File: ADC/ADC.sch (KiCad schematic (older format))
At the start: 89 parts

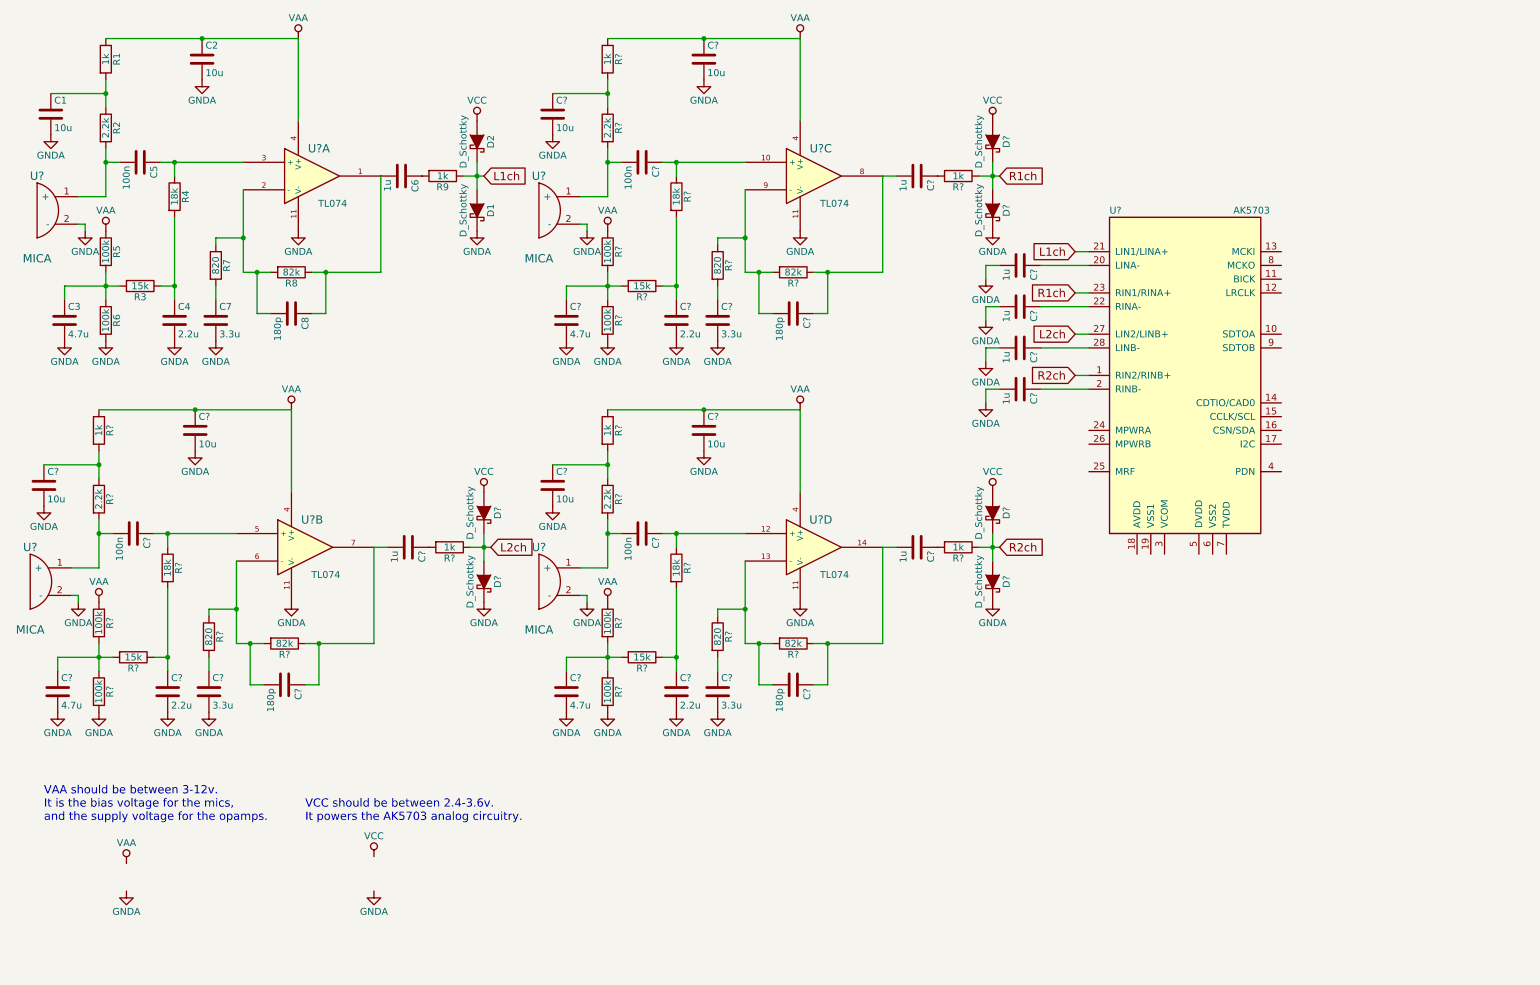
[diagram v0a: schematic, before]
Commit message: Finished Digital Section
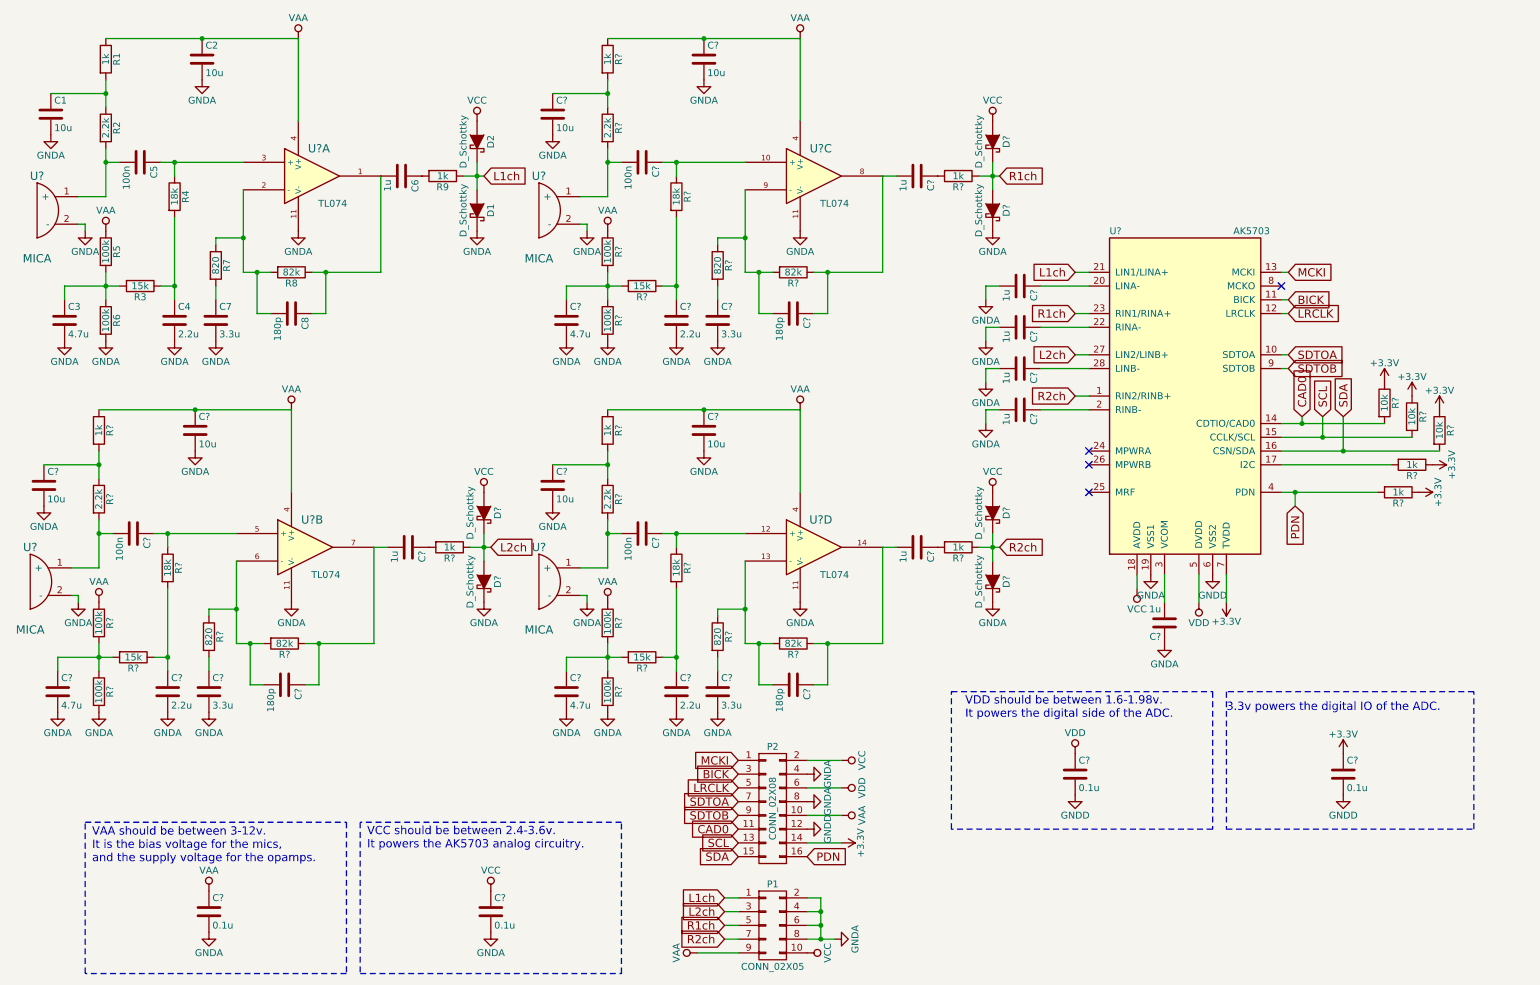
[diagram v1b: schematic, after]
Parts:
- added C?: 1u, symbol C
- added C? (x4): 0.1u, symbol C
- added P1: CONN_02X05, symbol CONN_02X05
- added P2: CONN_02X08, symbol CONN_02X08
- added R? (x2): 1k, symbol R
- added R? (x3): 10k, symbol R
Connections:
- net GNDA: now also U?.19 (VSS1), C?.1, C?.2, C?.2, P1.2 (P2), P1.4 (P4), P1.6 (P6), P1.8 (P8), P2.4 (P4), P2.8 (P8)
- net L1ch: now also P1.1 (P1)
- net L2ch: now also P1.3 (P3)
- net R1ch: now also P1.5 (P5)
- net R2ch: now also P1.7 (P7)
- net VAA: now also C?.1, P1.9 (P9), P2.10 (P10)
- net VCC: now also U?.18 (AVDD), C?.1, P1.10 (P10), P2.2 (P2)
- net SDTOA: now reaches U?.10 (SDTOA)
- net SDTOA: now also P2.7 (P7)
- net BICK: now reaches U?.11 (BICK)
- net BICK: now also P2.3 (P3)
- net LRCLK: now reaches U?.12 (LRCLK)
- net LRCLK: now also P2.5 (P5)
- net MCKI: now reaches U?.13 (MCKI)
- net MCKI: now also P2.1 (P1)
- net CAD0: now reaches U?.14 (CDTIO/CAD0)
- net CAD0: now also P2.11 (P11), R?.2
- net SCL: now reaches U?.15 (CCLK/SCL)
- net SCL: now also P2.13 (P13), R?.2
- net SDA: now reaches U?.16 (CSN/SDA)
- net SDA: now also P2.15 (P15), R?.2
- net at U?.17 (I2C): now also R?.2
- net at U?.3 (VCOM): now also C?.2
- net PDN: now reaches U?.4 (PDN)
- net PDN: now also P2.16 (P16), R?.2
- net VDD: now reaches U?.5 (DVDD)
- net VDD: now also C?.1, P2.6 (P6)
- net GNDD: now reaches U?.6 (VSS2)
- net GNDD: now also C?.2, C?.2, P2.12 (P12)
- net +3V3: now reaches U?.7 (TVDD)
- net +3V3: now also C?.1, P2.14 (P14), R?.1, R?.1, R?.1, R?.1, R?.1
- net SDTOB: now reaches U?.9 (SDTOB)
- net SDTOB: now also P2.9 (P9)
- no-connect marks 0 -> 4
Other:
- note added: "3.3v powers the digital IO of the ADC."
- note added: "VDD should be between 1.6-1.98v.\nIt powers the digital side of the ADC."
- moved on the sheet: C?, U?

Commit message: Schematic complete, need footprint for mic
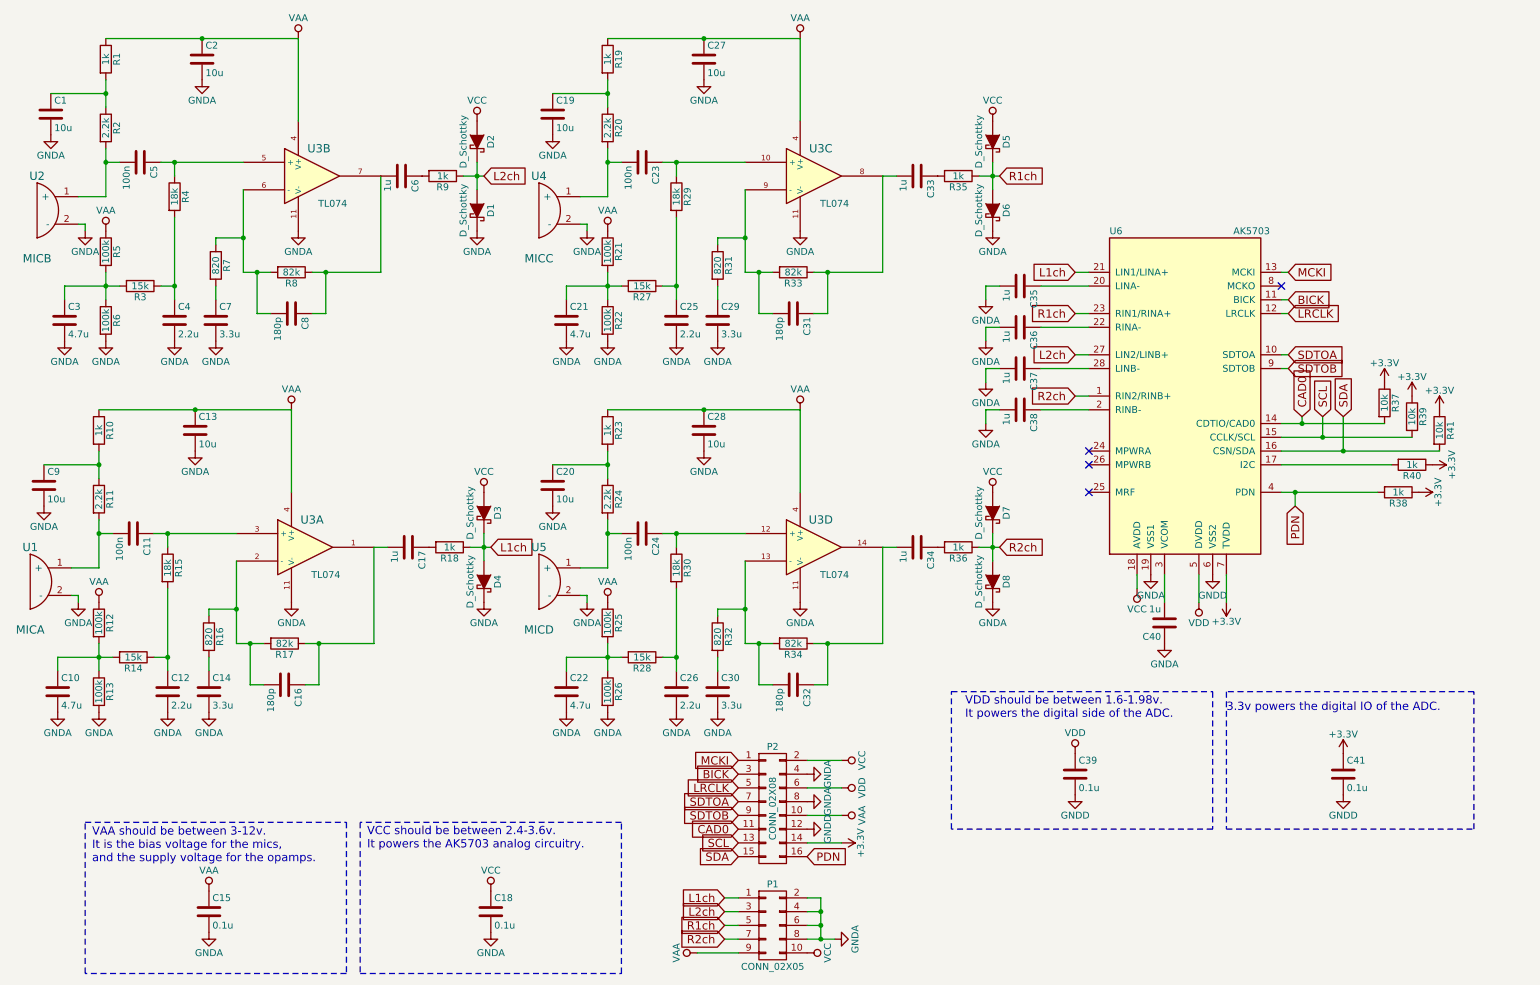
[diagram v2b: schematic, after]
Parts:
- C1, C2, C3, C4, C5, C6, C7, C8: footprint (none) -> Capacitors_SMD:C_0603_HandSoldering
- C10, C11, C12, C13, C14, C15, C16, C17, C18, C19, C20, C21, C22, C23, C24, C25, C26, C27, C28, C29, C30, C31, C32, C33, C34, C35, C36, C37, C38, C39, C40, C41, C9: renamed from C?; footprint (none) -> Capacitors_SMD:C_0603_HandSoldering
- D1, D2: footprint (none) -> Diodes_ThroughHole:Diode_DO-41_SOD81_Horizontal_RM10
- D3, D4, D5, D6, D7, D8: renamed from D?; footprint (none) -> Diodes_ThroughHole:Diode_DO-41_SOD81_Horizontal_RM10
- P1: footprint (none) -> Pin_Headers:Pin_Header_Straight_2x05
- P2: footprint (none) -> Pin_Headers:Pin_Header_Straight_2x08
- R1, R2, R3, R4, R5, R6, R7, R8, R9: footprint (none) -> Resistors_SMD:R_0603_HandSoldering
- R10, R11, R12, R13, R14, R15, R16, R17, R18, R19, R20, R21, R22, R23, R24, R25, R26, R27, R28, R29, R30, R31, R32, R33, R34, R35, R36, R37, R38, R39, R40, R41: renamed from R?; footprint (none) -> Resistors_SMD:R_0603_HandSoldering
- U2: renamed from U?; value MICA -> MICB
- U3: renamed from U?; footprint (none) -> Housings_SSOP:TSSOP-14_4.4x5mm_Pitch0.65mm
- U4: renamed from U?; value MICA -> MICC
- U5: renamed from U?; value MICA -> MICD
- U6: renamed from U?; footprint (none) -> Housings_DFN_QFN:QFN-28-1EP_4x4mm_Pitch0.4mm
- gave numbers to parts that had none: 1
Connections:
- net L1ch: now also D3.2 (K), D4.1 (A), R18.1; no longer D1.1 (A), D2.2 (K), R9.1
- net L2ch: now also D1.1 (A), D2.2 (K), R9.1; no longer D3.2 (K), D4.1 (A), R18.1
- net at C6.2, C8.1, R8.1: now also U3.7; no longer U3.1
- net at C8.2, R7.1, R8.2: now also U3.6 (-); no longer U3.2 (-)
- net at C5.1, R4.1: now also U3.5 (+); no longer U3.3 (+)
- net at C11.1, R15.1: now also U3.3 (+); no longer U3.5 (+)
- net at C16.2, R16.1, R17.2: now also U3.2 (-); no longer U3.6 (-)
- net at C16.1, C17.2, R17.1: now also U3.1; no longer U3.7

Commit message: Added freeroute and the first pass at a PCB
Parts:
- U1, U2, U4, U5: footprint (none) -> Buzzers_Beepers:MagneticBuzzer_Kingstate_KCG0601
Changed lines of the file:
@@
 LIBS:adcparts
 LIBS:microphone
+LIBS:ADC-cache
 EELAYER 25 0
 EELAYER END
@@
 F 0 "U2" H 650 2250 60  0000 C CNN
 F 1 "MICB" H 650 1650 60  0000 C CNN
-F 2 "" H 650 2000 60  0001 C CNN
+F 2 "Buzzers_Beepers:MagneticBuzzer_Kingstate_KCG0601" H 650 2000 60  0001 C CNN
 F 3 "" H 650 2000 60  0000 C CNN
 	1    650  2000
@@
 F 0 "U1" H 600 4950 60  0000 C CNN
 F 1 "MICA" H 600 4350 60  0000 C CNN
-F 2 "" H 600 4700 60  0001 C CNN
+F 2 "Buzzers_Beepers:MagneticBuzzer_Kingstate_KCG0601" H 600 4700 60  0001 C CNN
 F 3 "" H 600 4700 60  0000 C CNN
 	1    600  4700
@@
 F 0 "U4" H 4300 2250 60  0000 C CNN
 F 1 "MICC" H 4300 1650 60  0000 C CNN
-F 2 "" H 4300 2000 60  0001 C CNN
+F 2 "Buzzers_Beepers:MagneticBuzzer_Kingstate_KCG0601" H 4300 2000 60  0001 C CNN
 F 3 "" H 4300 2000 60  0000 C CNN
 	1    4300 2000
@@
 F 0 "U5" H 4300 4950 60  0000 C CNN
 F 1 "MICD" H 4300 4350 60  0000 C CNN
-F 2 "" H 4300 4700 60  0001 C CNN
+F 2 "Buzzers_Beepers:MagneticBuzzer_Kingstate_KCG0601" H 4300 4700 60  0001 C CNN
 F 3 "" H 4300 4700 60  0000 C CNN
 	1    4300 4700

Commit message: matlab files
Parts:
- D1, D2, D3, D4, D5, D6, D7, D8: symbol D_Schottky -> D_Schottky-RESCUE-ADC
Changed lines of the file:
@@
 EESchema Schematic File Version 2
+LIBS:ADC-rescue
 LIBS:power
 LIBS:device
@@
 VAA should be between 3-12v.\nIt is the bias voltage for the mics,\nand the supply voltage for the opamps.
 $Comp
-L D_Schottky D2
+L D_Schottky-RESCUE-ADC D2
 U 1 1 56412DA4
 P 3850 1500
@@
 $EndComp
 $Comp
-L D_Schottky D1
+L D_Schottky-RESCUE-ADC D1
 U 1 1 56412F07
 P 3850 2000
@@
 VCC should be between 2.4-3.6v.\nIt powers the AK5703 analog circuitry.
 $Comp
-L D_Schottky D3
+L D_Schottky-RESCUE-ADC D3
 U 1 1 564163F3
 P 3900 4200
@@
 $EndComp
 $Comp
-L D_Schottky D4
+L D_Schottky-RESCUE-ADC D4
 U 1 1 564163F9
 P 3900 4700
@@
 $EndComp
 $Comp
-L D_Schottky D5
+L D_Schottky-RESCUE-ADC D5
 U 1 1 56416B6F
 P 7600 1500
@@
 $EndComp
 $Comp
-L D_Schottky D6
+L D_Schottky-RESCUE-ADC D6
 U 1 1 56416B75
 P 7600 2000
@@
 $EndComp
 $Comp
-L D_Schottky D7
+L D_Schottky-RESCUE-ADC D7
 U 1 1 564174BA
 P 7600 4200
@@
 $EndComp
 $Comp
-L D_Schottky D8
+L D_Schottky-RESCUE-ADC D8
 U 1 1 564174C0
 P 7600 4700
